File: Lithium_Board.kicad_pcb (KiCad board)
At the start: 6 copper layers, 80 x 67 mm, 117 parts, among them IC1 BQ25750RRVR, IC2 TPS70933DBVR, IC4 STM32G0B1CBT6N, IC5 TCAN3414DR, IC6 BQ7694204PFBR, J1 XT30PW-M, J2 XT30PW-F, J3 XT30PW-M, J4 S3B-XH-SM4-TB_LF__SN_, J5 TSW-105-07-G-S, J6 Conn_01x06, J7 Conn_01x04, Q1 SIR870ADP-T1-GE3, Q10 MMBT5551LT1G, Q2 SIR870ADP-T1-GE3, Q3 SIR870ADP-T1-GE3, Q4 SIR870ADP-T1-GE3, Q5 SIR870ADP-T1-GE3, Q6 SIR870ADP-T1-GE3, Q7 SIR870ADP-T1-GE3, Q8 SIR870ADP-T1-GE3

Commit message: Final PERFECT design before big changes
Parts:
- R24: value 10k -> 1k; footprint RC0603FR-0710KL:RESC1608X55N -> RC0603FR-071KL:RESC1608X55N
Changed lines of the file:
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@@
 		(property "Reference" "D2"
 			(at 0 0 90)
-			(layer "B.SilkS")
+			(layer "F.SilkS")
 			(effects
 				(font
-					(size 1 1)
-					(thickness 0.153)
+					(size 1.27 1.27)
+					(thickness 0.254)
 				)
-				(justify mirror)
 			)
 		)
@@
 		(fp_text user "${REFERENCE}"
 			(at 0 0 90)
-			(layer "B.Fab")
+			(layer "F.Fab")
 			(effects
 				(font
-					(size 1 1)
-					(thickness 0.153)
+					(size 1.27 1.27)
+					(thickness 0.254)
 				)
-				(justify mirror)
 			)
 		)
@@
 		)
 	)
-	(footprint "RC0603FR-0710KL:RESC1608X55N"
+	(footprint "RC0603FR-071KL:RESC1608X55N"
 		(layer "F.Cu")
 		(at 150.692946 97.62 90)
@@
 		(tags "Resistor")
 		(property "Reference" "R24"
-			(at 0 0 270)
+			(at 0 0 -90)
 			(layer "B.SilkS")
 			(effects
@@
 			)
 		)
-		(property "Value" "10k"
+		(property "Value" "1k"
 			(at 0 0 90)
 			(layer "F.SilkS")
@@
 			)
 		)
-		(property "Datasheet" "http://www.yageo.com/documents/recent/PYu-RC0603_51_RoHS_L_v5.pdf"
+		(property "Datasheet" "https://www.yageo.com/upload/media/product/productsearch/datasheet/rchip/PYu-RC_Group_51_RoHS_L_12.pdf"
 			(at 0 0 90)
 			(layer "F.Fab")
@@
 			)
 		)
-		(property "Description" "Yageo RC Series Thick Film Surface Mount Resistor 0603 Case 10k"
+		(property "Description" "Res Thick Film 0603 1K Ohm 1% 0.1W(1/10W) +/-100ppm/C Epoxy Pad SMD T/R"
 			(at 0 0 90)
 			(layer "F.Fab")
@@
 			)
 		)
-		(property "Mouser Part Number" "603-RC0603FR-0710KL"
+		(property "Mouser Part Number" "603-RC0603FR-071KL"
 			(at 0 0 90)
 			(unlocked yes)
@@
 			)
 		)
-		(property "Mouser Price/Stock" "https://www.mouser.co.uk/ProductDetail/YAGEO/RC0603FR-0710KL?qs=grNVn54RoB%252B3GtjbJj3wJQ%3D%3D"
+		(property "Mouser Price/Stock" "https://www.mouser.co.uk/ProductDetail/YAGEO/RC0603FR-071KL?qs=VU8sRB4EgwApHsk4rF%2F3zg%3D%3D"
 			(at 0 0 90)
 			(unlocked yes)
@@
 			)
 		)
-		(property "Manufacturer_Part_Number" "RC0603FR-0710KL"
+		(property "Manufacturer_Part_Number" "RC0603FR-071KL"
 			(at 0 0 90)
 			(unlocked yes)
@@
 		)
 		(fp_text user "${REFERENCE}"
-			(at 0 0 270)
+			(at 0 0 -90)
 			(layer "B.Fab")
 			(effects
@@
 		)
 		(embedded_fonts no)
-		(model "RC0603FR-0710KL.stp"
+		(model "RC0603FR-071KL.stp"
 			(offset
-				(xyz 0 0 0.2300000007)
+				(xyz 0 0 0)
 			)
 			(scale
@@
 		(property "Reference" "D5"
 			(at 0 0 90)
-			(layer "B.SilkS")
+			(layer "F.SilkS")
 			(effects
 				(font
-					(size 1 1)
-					(thickness 0.153)
+					(size 1.27 1.27)
+					(thickness 0.254)
 				)
-				(justify mirror)
 			)
 		)
@@
 		(fp_text user "${REFERENCE}"
 			(at 0 0 90)
-			(layer "B.Fab")
+			(layer "F.Fab")
 			(effects
 				(font
-					(size 1 1)
-					(thickness 0.153)
+					(size 1.27 1.27)
+					(thickness 0.254)
 				)
-				(justify mirror)
 			)
 		)

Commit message: New Placement and Polygons
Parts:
- C14, C15, C21, C27, C28, IC4, LED1, LED2, R26, R31, R34: moved to B.Cu
- moved G*** 79.6 mm to (146.8, 26.2)
- moved G*** 79.3 mm to (146.8, 26.4)
- moved G*** 60.8 mm to (159.4, 25.9)
- moved G*** 39.2 mm to (167.4, 26.1)
- moved R1 36.7 mm to (130.0, 84.2)
- moved R3 32.2 mm to (132.3, 82.7)
- moved C21 32.1 mm to (135.6, 103.7), turned to 180 degrees
- moved C14 27.4 mm to (135.3, 108.5)
- moved Q8 26.4 mm to (157.5, 74.9), turned to 180 degrees
- moved R9 24.2 mm to (152.6, 91.1), turned to 0 degrees
- moved C28 22.7 mm to (137.8, 106.0)
- moved C27 22.6 mm to (137.8, 108.7)
- moved Z1 22.6 mm to (119.5, 70.2), turned to -90 degrees
- moved R11 21.9 mm to (152.7, 92.7), turned to 180 degrees
- moved Q6 21.4 mm to (130.1, 70.1), turned to 0 degrees
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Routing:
- net GND: track 98.6 -> 0.00 mm, vias 166 -> 82
- net BQ_TS: track 70.4 -> 7.17 mm, vias 1 -> 0
- net /Q1_D: track 54.0 -> 0.00 mm, vias 2 -> 0
- net BQ2_ALERT: track 48.4 -> 0.00 mm, vias 2 -> 0
- net BQ2_SCLK: track 42.0 -> 0.00 mm, vias 2 -> 0
- net BQ2_MISO: track 41.4 -> 0.00 mm, vias 2 -> 0
- net BQ2_MOSI: track 40.5 -> 0.00 mm, vias 2 -> 0
- net BQ_SCL: track 47.9 -> 9.04 mm, vias 2 -> 0
- net BQ_SDA: track 46.4 -> 8.28 mm, vias 2 -> 0
- net BQ2_CS: track 36.2 -> 0.00 mm, vias 2 -> 0
- net BQ_BATDRV: track 34.1 -> 0.00 mm, vias 2 -> 0
- net /ACDRV: track 32.8 -> 0.00 mm
- net /ACN: track 43.8 -> 11.2 mm, vias 2 -> 0
- net /HIDRV2: track 31.8 -> 0.00 mm, vias 2 -> 0
- net /VAC: track 31.7 -> 0.00 mm
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- added copper zone on B.Cu, net +3V3
- added copper zone on In3.Cu, net BQ_SYS
- removed copper zone on In2.Cu, net +BATT
- removed copper zone on F.Cu, net /Q1_D
- removed copper zone on F.Cu, net /Q4_S
- removed copper zone on In3.Cu, net /Q4_S
- removed copper zone on B.Cu, net /Q7_DRAIN
- removed copper zone on F.Cu, net /Q7_DRAIN
- removed copper zone on In2.Cu, net /SW1
- removed copper zone on In3.Cu, net /SW2
- removed copper zone on F.Cu, net BQ_BATSRC
- removed copper zone on In3.Cu, net BQ_BATSRC
- removed copper zone on In2.Cu, net BQ_SYS

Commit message: LITHIUM V2 Placement
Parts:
- moved R41 4.25 mm to (113.8, 83.5)
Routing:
- net BQ_TS: track 7.17 -> 64.4 mm, vias 0 -> 1
- net +BATT: track 0.00 -> 30.2 mm, vias 9 -> 12
- net BQ2_CS: track 0.00 -> 29.5 mm, vias 0 -> 2
- net /CELL BALANCING IC/VC(3-9): track 0.00 -> 29.1 mm, vias 0 -> 2
- net BQ2_MOSI: track 0.00 -> 25.3 mm, vias 0 -> 1
- net BQ_SCL: track 9.04 -> 33.7 mm, vias 0 -> 2
- net BAT1: track 0.00 -> 24.4 mm, vias 0 -> 1
- net BQ2_MISO: track 0.00 -> 24.4 mm, vias 0 -> 1
- net BQ2_ALERT: track 0.00 -> 24.0 mm, vias 0 -> 1
- net BQ2_SCLK: track 0.00 -> 23.4 mm, vias 0 -> 1
- net BQ_SDA: track 8.28 -> 31.3 mm, vias 0 -> 2
- net CAN_STB: track 0.00 -> 22.4 mm, vias 0 -> 1
- net /HIDRV2: track 0.00 -> 22.3 mm, vias 0 -> 2
- net BQ_LODRV2: track 0.00 -> 21.9 mm, vias 0 -> 2
- net Net-(D4-K): track 0.00 -> 20.7 mm, vias 0 -> 2
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- added copper zone on In2.Cu, net +BATT
- added copper zone on F.Cu, net /Q7_DRAIN
- added copper zone on In2.Cu, net /Q7_DRAIN

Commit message: Final LITHIUM Design V2
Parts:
- moved G*** 88.7 mm to (157.7, 114.5)
- moved G*** 85.4 mm to (125.6, 109.0)
- moved G*** 61.3 mm to (111.1, 63.7)
- moved G*** 39.3 mm to (178.0, 63.9)
- moved Z1 7.35 mm to (126.8, 70.3), turned to 90 degrees
- moved Q1 2.62 mm to (124.6, 71.2)
- moved Q4 2.40 mm to (119.7, 68.5)
- moved C1 0.96 mm to (115.3, 70.3)
- moved R6 0.92 mm to (117.7, 73.8)
- moved R4 0.46 mm to (115.2, 74.1)
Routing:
- net GND: track 0.00 -> 63.6 mm, vias 82 -> 139
- net /ACDRV: track 0.00 -> 33.3 mm, vias 0 -> 2
- net /VAC: track 0.00 -> 31.7 mm, vias 0 -> 2
- net +BATT: track 30.2 -> 0.00 mm, vias 12 -> 15
- net BQ_BATDRV: track 0.00 -> 28.7 mm, vias 0 -> 2
- net BQ_ACUV: track 7.00 -> 33.7 mm
- net BQ_BATSRC: track 0.00 -> 25.2 mm, vias 0 -> 7
- net Net-(C22-Pad1): track 0.00 -> 4.41 mm
- net Net-(R12-Pad1): track 0.00 -> 1.80 mm
- net BQ_ACOV: track 7.46 -> 9.16 mm
- net BQ_SYS: track 5.87 -> 7.22 mm
- net BQ2_CS: vias 2 -> 1
- net /Q4_S: vias 0 -> 5
- net /Q1_D: vias 0 -> 9
- net +3V3: vias 22 -> 24
- added copper zone on F.Cu, net /Q1_D
- added copper zone on In2.Cu, net /Q1_D
- added copper zone on F.Cu, net /Q4_S
- added copper zone on In2.Cu, net /Q4_S
- added copper zone on B.Cu, net BQ_BATSRC
- added copper zone on F.Cu, net BQ_BATSRC
- added copper zone on B.Cu, net GND

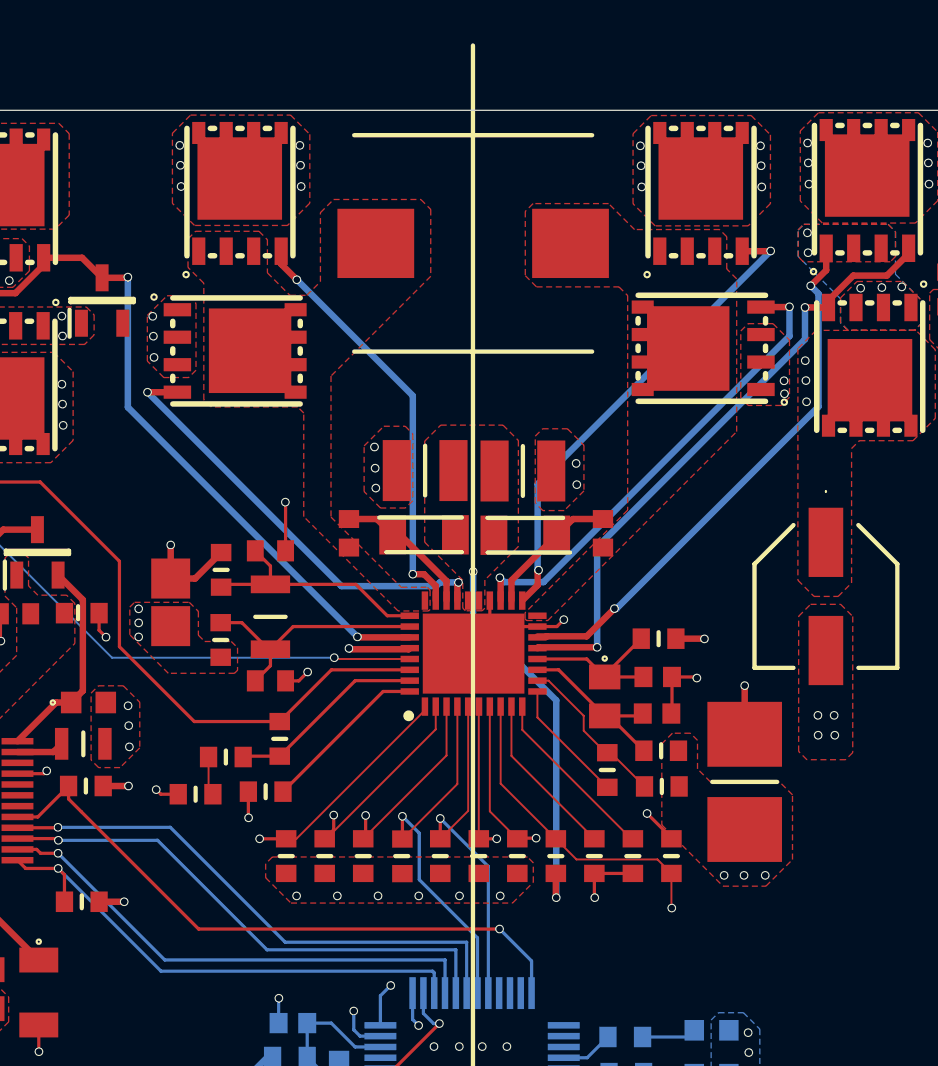
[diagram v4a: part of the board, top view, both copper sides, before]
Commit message: Differential Routing
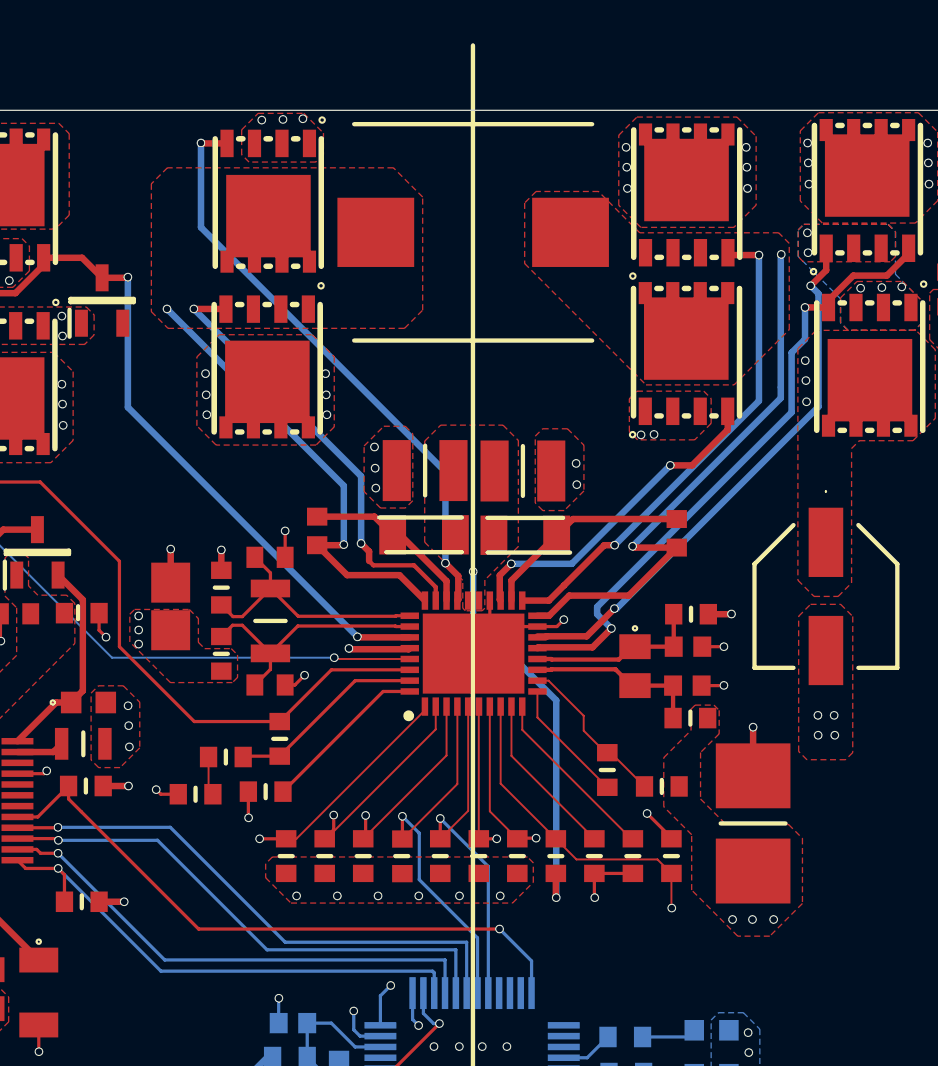
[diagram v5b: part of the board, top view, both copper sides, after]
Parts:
- moved Q6 10.1 mm to (136.9, 62.8), turned to -90 degrees
- moved Q5 6.56 mm to (136.9, 70.4), turned to -90 degrees
- moved Q8 6.14 mm to (151.4, 75.6), turned to 90 degrees
- moved C5 3.41 mm to (153.4, 81.0)
- moved R9 2.03 mm to (154.0, 89.6)
- moved C9 1.98 mm to (151.4, 87.2)
- moved C10 1.98 mm to (153.9, 86.3)
- moved R7 1.96 mm to (156.9, 94.4)
- moved C13 1.90 mm to (153.8, 88.1)
- moved R5 1.88 mm to (154.0, 84.8)
- moved C4 1.47 mm to (136.7, 80.9)
- moved R3 0.82 mm to (132.3, 83.5)
- moved Q2 0.66 mm to (151.4, 68.3)
- moved R2 0.64 mm to (132.3, 86.6)
- moved L1 0.51 mm to (143.9, 67.1)
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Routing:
- net /SW2: track 0.00 -> 26.1 mm, vias 0 -> 2
- net /SW1: track 0.00 -> 21.6 mm, vias 0 -> 2
- net BQ_LODRV1: track 20.4 -> 27.3 mm
- net BQ_LODRV2: track 21.9 -> 15.4 mm
- net /BTST2: track 6.34 -> 9.75 mm
- net GND: track 63.6 -> 61.6 mm, vias 139 -> 140
- net BQ_SYS: track 7.22 -> 5.34 mm, vias 32 -> 33
- net /BTST1: track 6.60 -> 8.11 mm
- net /HIDRV1: track 19.4 -> 20.7 mm
- net /HIDRV2: track 22.3 -> 23.0 mm
- net /ACN: track 11.2 -> 11.8 mm

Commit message: CANBUS FIXED
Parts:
- moved R30 0.61 mm to (123.6, 115.7)
- moved R29 0.60 mm to (123.6, 118.2)
- moved C24 0.39 mm to (123.8, 117.0)
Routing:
- net GND: track 61.6 -> 59.3 mm
- net Net-(C24-Pad1): track 3.89 -> 2.51 mm
- net /CANBUS/CAN_P: track 13.9 -> 15.2 mm
- net /CANBUS/CAN_N: track 14.1 -> 15.3 mm

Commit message: Perfected Polygons
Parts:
- moved C1 4.05 mm to (114.0, 74.1), turned to -90 degrees
- moved C22 1.99 mm to (170.2, 64.6)
- moved C7 1.47 mm to (115.9, 79.4)
- moved R7 1.16 mm to (156.9, 95.6)
- moved J2 1.09 mm to (110.7, 76.1)
- moved R4 0.76 mm to (115.9, 74.2)
- moved R6 0.20 mm to (117.9, 73.9)
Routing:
- net +BATT: track 0.00 -> 13.7 mm, vias 15 -> 29
- net BQ_SYS: track 5.34 -> 2.85 mm, vias 33 -> 49
- net Net-(C22-Pad1): track 4.41 -> 6.83 mm
- net /Q7_DRAIN: track 3.32 -> 1.07 mm, vias 11 -> 28
- net /VAC: track 31.7 -> 33.6 mm
- net /CANBUS/CAN_N: track 15.3 -> 13.8 mm
- net /CANBUS/CAN_P: track 15.2 -> 13.7 mm
- net GND: track 59.3 -> 58.2 mm, vias 140 -> 151
- net /Q1_D: vias 9 -> 18
- net +3V3: vias 24 -> 35

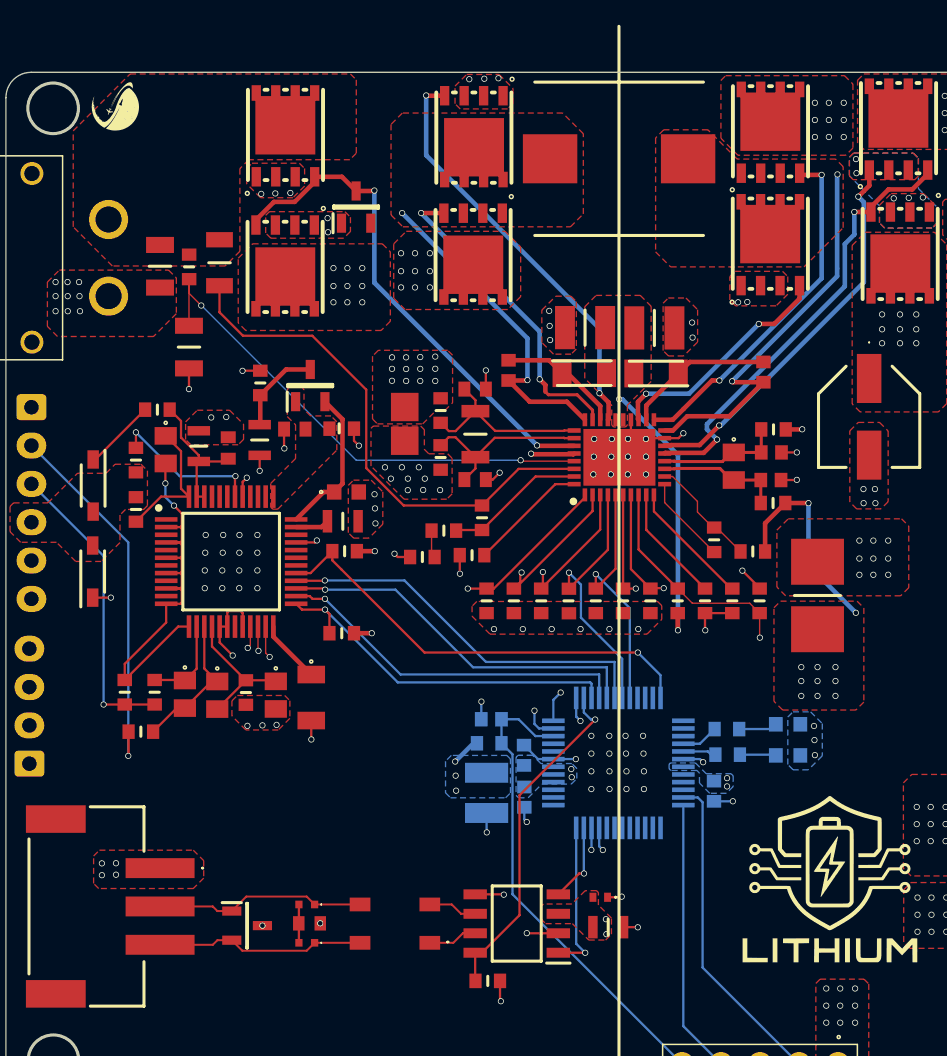
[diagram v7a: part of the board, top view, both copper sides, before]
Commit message: Added Return Vias
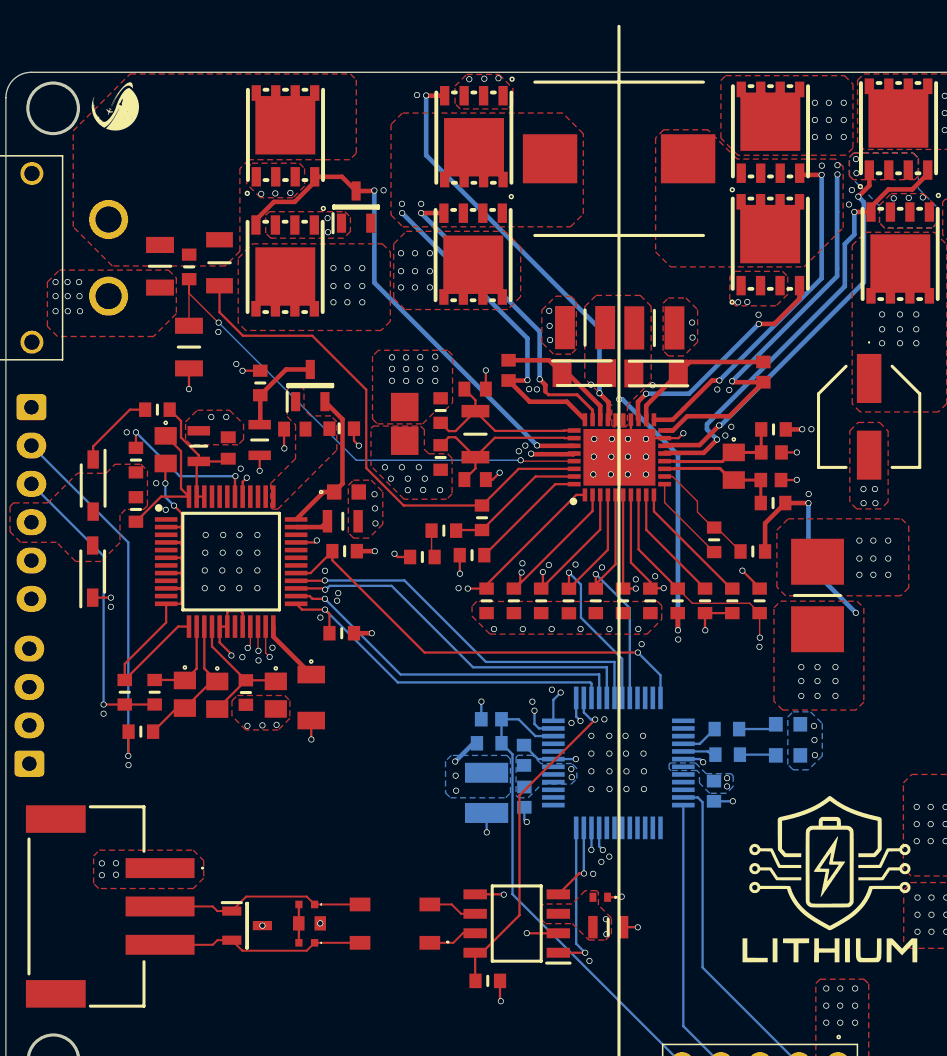
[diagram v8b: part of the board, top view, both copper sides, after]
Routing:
- net BQ_TS: track 64.4 -> 66.7 mm
- net GND: vias 151 -> 206
